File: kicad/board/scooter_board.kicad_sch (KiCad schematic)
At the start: 39 parts, among them J3 Amphenol 98424-F52-12ALF, J4 OLED I2C JST-GH RA, J6 EXP D10/SDA/SCL/5V/3V3/GND/PA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, Q1 2N7002, U2 LSM6DS3TR-C, U3 XIAO ESP32-C3

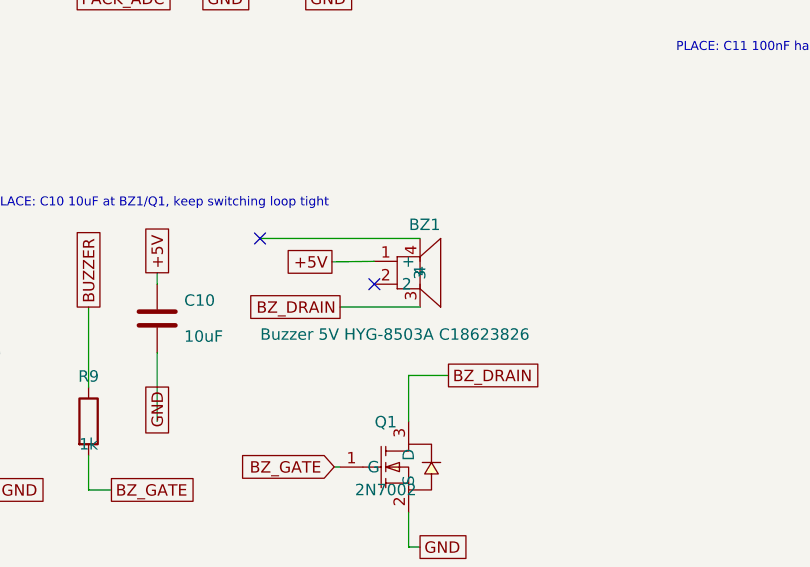
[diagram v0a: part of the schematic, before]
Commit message: Fix buzzer: route BZ_DRAIN to footprint pad 2
The HYG-8503A symbol mapped BZ_DRAIN to pad 3, but the buzzer's - terminal
is pad 2, so the gate drive never reached the buzzer (scope showed a clean
2.7 kHz square on the Q1 gate with nothing switching at the buzzer). Swap
the symbol's lower pin numbers 2<->3 in both the LCSC library and the
schematic's cached copy so BZ_DRAIN lands on pad 2, then update the PCB
netlist and re-route the track.

Co-Authored-By: Claude Opus 4.8 <noreply@anthropic.com>
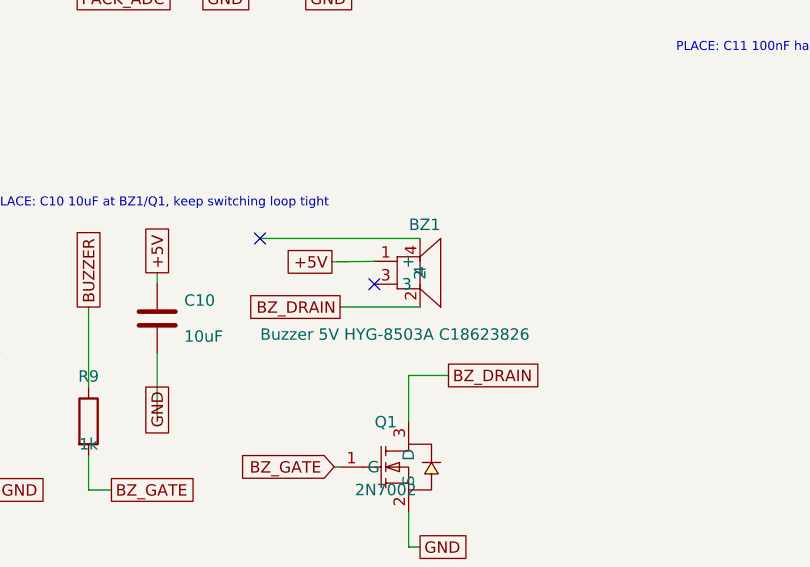
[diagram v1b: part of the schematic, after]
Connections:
- net BZ_DRAIN: now also BZ1.2; no longer BZ1.3
